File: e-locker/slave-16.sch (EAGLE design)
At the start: 85 parts, among them IC1 PCF8574P, IC2 PCF8574P, IC3 PCF8574P, IC4 PCF8574P, X1 JST-XH-02-PIN-LONG-PAD, X10 JST-XH-04-PIN-LONG-PAD, X11 JST-XH-02-PIN-LONG-PAD, X12 JST-XH-04-PIN-LONG-PAD, X13 JST-XH-04-PIN-LONG-PAD, X14 JST-XH-04-PIN-LONG-PAD, X15 JST-XH-04-PIN-LONG-PAD, X16 JST-XH-04-PIN-LONG-PAD, X17 JST-XH-04-PIN-LONG-PAD, X18 JST-XH-04-PIN-LONG-PAD, X19 JST-XH-04-PIN-LONG-PAD, X2 JST-XH-05-PIN-LONG-PAD, X20 JST-XH-05-PIN-LONG-PAD, X21 JST-XH-02-PIN-LONG-PAD, X22 JST-XH-02-PIN-LONG-PAD, X3 JST-XH-04-PIN-LONG-PAD, X4 JST-XH-04-PIN-LONG-PAD, X5 JST-XH-04-PIN-LONG-PAD, X6 JST-XH-04-PIN-LONG-PAD, X7 JST-XH-04-PIN-LONG-PAD, X8 JST-XH-04-PIN-LONG-PAD, X9 JST-XH-04-PIN-LONG-PAD

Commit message: arduino footprint change
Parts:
- removed U$11: PRO-MINI, Arduino-clone:PRO-MINI
- added U$20: PRO-MINI-2, Arduino-clone:PRO-MINI-2
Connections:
- removed net A6: U$11.A6
- net A0: now also U$20.A0; no longer U$11.A0
- net A1: now also U$20.A1; no longer U$11.A1
- net A2: now also U$20.A2; no longer U$11.A2
- net A3: now also U$20.A3; no longer U$11.A3
- net A4: now also U$20.A4; no longer U$11.A4
- net A5: now also U$20.A5; no longer U$11.A5
- net A7: now also U$20.A7; no longer U$11.A7
- net D0: now also U$20.RX1; no longer U$11.RX1
- net D1: now also U$20.TX0; no longer U$11.TX0
- net D11: now also U$20.D11; no longer U$11.D11
- net D12: now also U$20.D12; no longer U$11.D12
- net D13: now also U$20.D13; no longer U$11.D13
- net GND: now also U$20.GND, U$20.GND2; no longer U$11.GND, U$11.GND2
- net N$10: now also U$20.D2; no longer U$11.D2
- net N$17: now also U$20.D3; no longer U$11.D3
- net N$20: now also U$20.D4; no longer U$11.D4
- net N$21: now also U$20.D5; no longer U$11.D5
- net N$22: now also U$20.D6; no longer U$11.D6
- net N$23: now also U$20.D7; no longer U$11.D7
- net N$24: now also U$20.D8; no longer U$11.D8
- net N$25: now also U$20.D9; no longer U$11.D9
- net RST: now also U$20.RST; no longer U$11.RST
- net VCC: now also U$20.VCC; no longer U$11.VCC

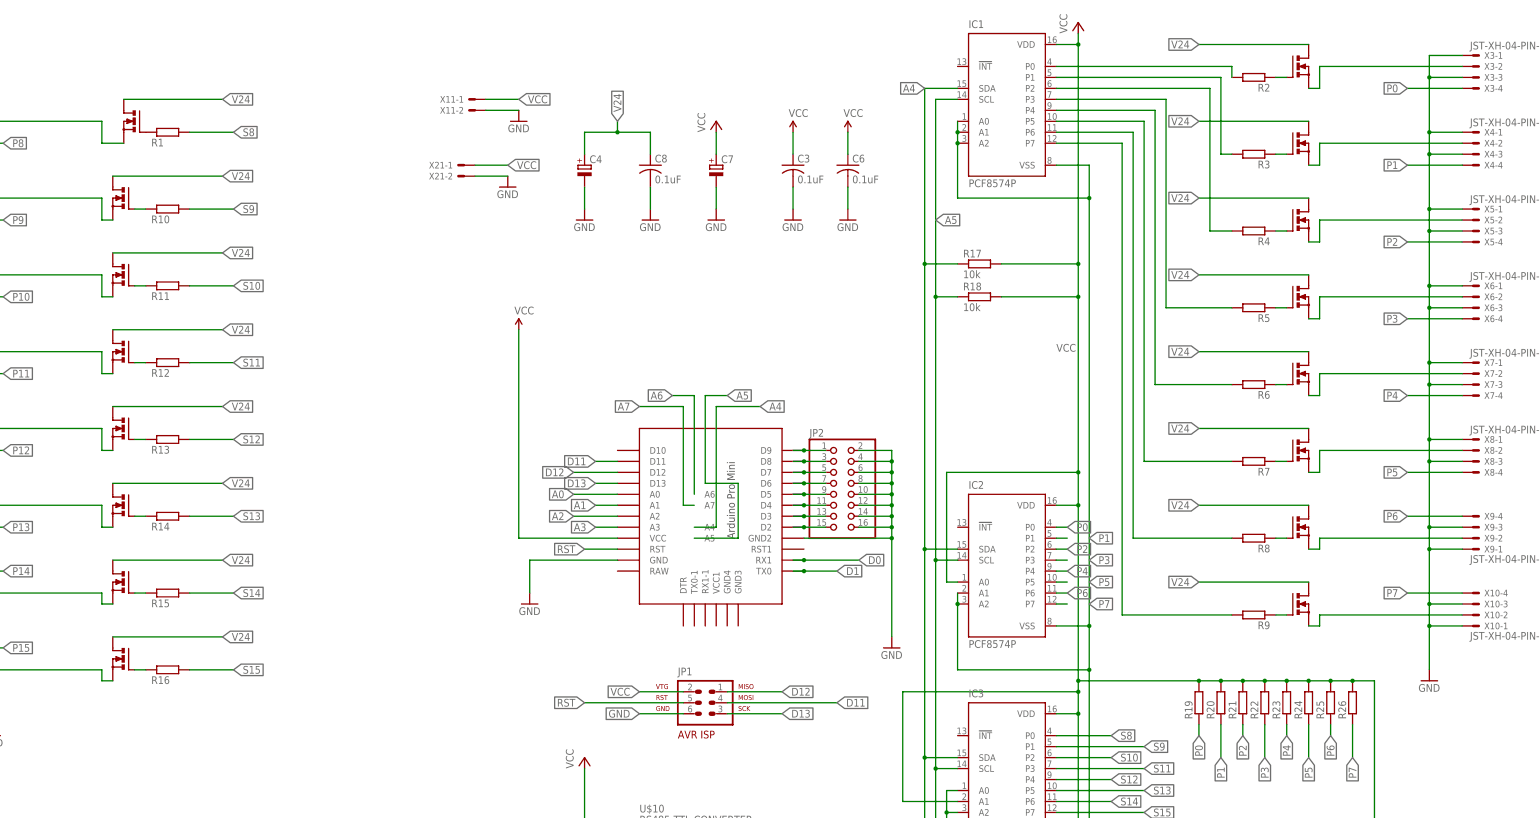
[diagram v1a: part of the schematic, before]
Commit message: slave p-channel mosfet
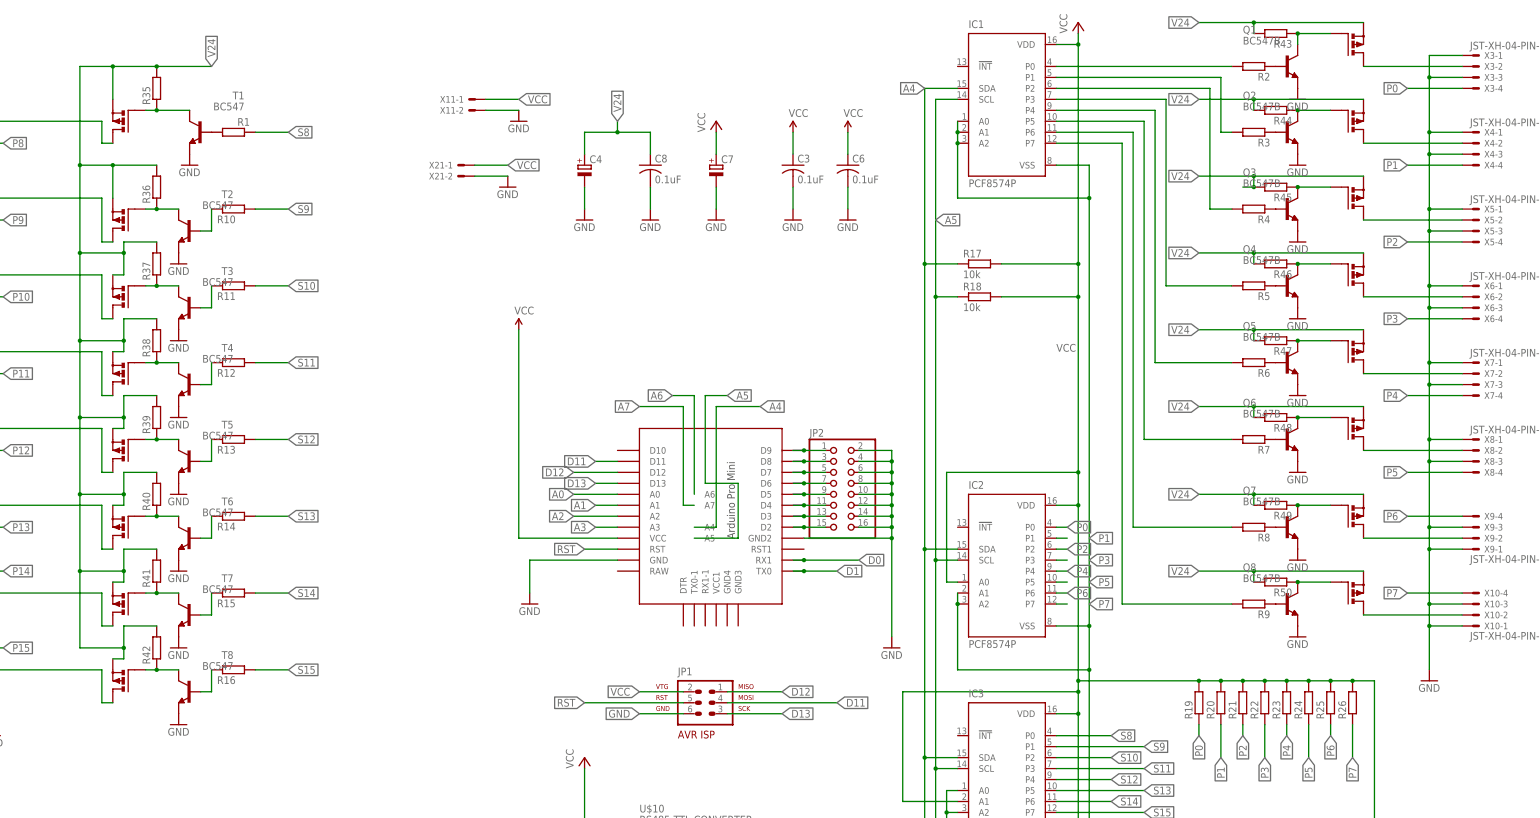
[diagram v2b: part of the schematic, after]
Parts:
- added Q1, Q2, Q3, Q4, Q5, Q6, Q7, Q8: BC547B, transistor-npn:BC547B
- added R35, R36, R37, R38, R39, R40, R41, R42, R43, R44, R45, R46, R47, R48, R49, R50: (no value), eagle-ltspice:RR1206
- added T1, T2, T3, T4, T5, T6, T7, T8: BC547, transistor:BC547
- U$1, U$12, U$13, U$14, U$15, U$16, U$17, U$18, U$19, U$2, U$3, U$4, U$5, U$6, U$7, U$8: value IRLML6344 -> IRLML6402; device mosfet:IRLML6344 -> mosfet:IRLML6402
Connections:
- new net A6: U$20.A6
- new net N$26: R1.2, T1.B
- new net N$27: R35.1, T1.C, U$12.G
- new net N$28: R42.1, T8.C, U$19.G
- new net N$29: R40.1, T6.C, U$17.G
- new net N$3: R15.1, T7.B
- new net N$54: U$8.D, X10-2.S
- new net N$55: R38.1, T4.C, U$15.G
- new net N$56: Q8.C, R50.1, U$8.G
- new net N$57: R12.1, T4.B
- new net N$58: R37.1, T3.C, U$14.G
- new net N$59: Q7.C, R49.1, U$7.G
- new net N$60: R11.1, T3.B
- new net N$61: R10.1, T2.B
- new net N$62: R36.1, T2.C, U$13.G
- new net N$63: Q6.C, R48.1, U$6.G
- new net N$64: Q5.C, R47.1, U$5.G
- net GND: now also Q1.E, Q2.E, Q3.E, Q4.E, Q5.E, Q6.E, Q7.E, Q8.E, T1.E, T2.E, T3.E, T4.E, T5.E, T6.E, T7.E, T8.E
- net N$1: now also Q8.B, R9.1; no longer R2.1, U$1.G
- net N$11: now also Q1.C, R43.1, U$1.G; no longer U$1.S, X3-2.S
- net N$12: now also Q2.C, R44.1, U$2.G; no longer U$2.S, X4-2.S
- net N$13: now also Q3.C, R45.1, U$3.G; no longer U$3.S, X5-2.S
- net N$14: now also Q4.C, R46.1, U$4.G; no longer U$4.S, X6-2.S
- net N$15: now also U$1.D, X3-2.S; no longer U$5.S, X7-2.S
- net N$16: now also U$2.D, X4-2.S; no longer U$6.S, X8-2.S
- net N$18: now also U$3.D, X5-2.S; no longer U$7.S, X9-2.S
- net N$19: now also U$4.D, X6-2.S; no longer U$8.S, X10-2.S
- net N$2: now also Q7.B, R8.1; no longer R3.1, U$2.G
- net N$38: now also R16.1, T8.B; no longer R1.1, U$12.G
- net N$39: now also R14.1, T6.B; no longer R10.1, U$13.G
- net N$4: now also Q6.B, R7.1; no longer R4.1, U$3.G
- net N$40: now also U$5.D, X7-2.S; no longer R11.1, U$14.G
- net N$41: now also U$6.D, X8-2.S; no longer R12.1, U$15.G
- net N$42: now also U$7.D, X9-2.S; no longer R13.1, U$16.G
- net N$43: now also R39.1, T5.C, U$16.G; no longer R14.1, U$17.G
- net N$44: now also R41.1, T7.C; no longer R15.1
- net N$45: now also R13.1, T5.B; no longer R16.1, U$19.G
- net N$46: now also U$12.D; no longer U$12.S
- net N$47: now also U$13.D; no longer U$13.S
- net N$48: now also U$14.D; no longer U$14.S
- net N$49: now also U$15.D; no longer U$15.S
- net N$5: now also Q5.B, R6.1; no longer R5.1, U$4.G
- net N$50: now also U$16.D; no longer U$16.S
- net N$51: now also U$17.D; no longer U$17.S
- net N$52: now also U$18.D; no longer U$18.S
- net N$53: now also U$19.D; no longer U$19.S
- net N$6: now also Q4.B, R5.1; no longer R6.1, U$5.G
- net N$7: now also Q3.B, R4.1; no longer R7.1, U$6.G
- net N$8: now also Q2.B, R3.1; no longer R8.1, U$7.G
- net N$9: now also Q1.B, R2.1; no longer R9.1, U$8.G
- net S8: now also R1.1; no longer R1.2
- net V24: now also R35.2, R36.2, R37.2, R38.2, R39.2, R40.2, R41.2, R42.2, R43.2, R44.2, R45.2, R46.2, R47.2, R48.2, R49.2, R50.2, U$1.S, U$12.S, U$13.S, U$14.S, U$15.S, U$16.S, U$17.S, U$18.S, U$19.S, U$2.S, U$3.S, U$4.S, U$5.S, U$6.S, U$7.S, U$8.S; no longer U$1.D, U$12.D, U$13.D, U$14.D, U$15.D, U$16.D, U$17.D, U$18.D, U$19.D, U$2.D, U$3.D, U$4.D, U$5.D, U$6.D, U$7.D, U$8.D
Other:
- moved on the sheet: R1, R10, R11, R12, R13, R14, R15, R16, R2, R3, R4, R5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
